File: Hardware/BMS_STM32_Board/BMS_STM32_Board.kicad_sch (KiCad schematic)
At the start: 46 parts, among them J1 Conn_01x05, J2 Conn_01x02, J3 Conn_01x04, J4 Conn_01x02, J5 Conn_01x04, Q1 Q_PMOS_GSD, U1 STM32F103C8Tx, U3 INA181, Y1 8MHz

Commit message: Hardware: footprint assignment complete
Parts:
- removed Q1: Q_PMOS_GSD, symbol Transistor_FET:Q_PMOS_GSD
- added Q1: Q_PMOS_GDS, Package_TO_SOT_SMD:TO-252-3_TabPin2, symbol Transistor_FET:Q_PMOS_GDS
- C1, C10, C11, C12, C13, C14, C15, C2, C3, C4, C6, C7, C8: footprint (none) -> Capacitor_SMD:C_0603_1608Metric
- C5: footprint (none) -> Capacitor_SMD:C_0805_2012Metric
- C9: footprint (none) -> Capacitor_THT:CP_Radial_D6.3mm_P2.50mm
- D1: footprint (none) -> Diode_SMD:D_SMA
- D2, D3, D4, D5: footprint (none) -> LED_SMD:LED_0805_2012Metric
- FB1: footprint (none) -> Inductor_SMD:L_0603_1608Metric
- J1: footprint (none) -> Connector_PinHeader_2.54mm:PinHeader_1x05_P2.54mm_Vertical
- J2, J4: footprint (none) -> TerminalBlock_Phoenix:TerminalBlock_Phoenix_MKDS-3-2-5.08_1x02_P5.08mm_Horizontal
- J3, J5: footprint (none) -> Connector:FanPinHeader_1x04_P2.54mm_Vertical
- R1, R10, R11, R12, R13, R14, R15, R2, R4, R5, R6, R7, R8, R9: footprint (none) -> Resistor_SMD:R_0603_1608Metric
- R3: footprint (none) -> Resistor_SMD:R_2512_6332Metric
- TH1: footprint (none) -> Connector_PinHeader_2.54mm:PinHeader_1x02_P2.54mm_Vertical
- Y1: footprint (none) -> Crystal:Crystal_SMD_3225-4Pin_3.2x2.5mm
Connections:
- net VIN_PROT: now also Q1.2 (D)
- net at R2.1: now also Q1.1 (G)
- net at J2.1 (Pin_1): now also Q1.3 (S)
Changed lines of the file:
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@@
 			)
 		)
-		(property "Footprint" ""
+		(property "Footprint" "Crystal:Crystal_SMD_3225-4Pin_3.2x2.5mm"
 			(at 107.95 73.66 0)
 			(hide yes)
@@
 			)
 		)
-		(property "Footprint" ""
+		(property "Footprint" "Resistor_SMD:R_0603_1608Metric"
 			(at 93.98 84.582 90)
 			(hide yes)
@@
 			)
 		)
-		(property "Footprint" ""
+		(property "Footprint" "Resistor_SMD:R_2512_6332Metric"
 			(at 58.42 103.378 90)
 			(hide yes)
@@
 			)
 		)
-		(property "Footprint" ""
+		(property "Footprint" "Resistor_SMD:R_0603_1608Metric"
 			(at 56.642 152.4 90)
 			(hide yes)
@@
 			)
 		)
-		(property "Footprint" ""
+		(property "Footprint" "Resistor_SMD:R_0603_1608Metric"
 			(at 115.062 54.61 90)
 			(hide yes)
@@
 			)
 		)
-		(property "Footprint" ""
+		(property "Footprint" "Connector:FanPinHeader_1x04_P2.54mm_Vertical"
 			(at 113.03 104.14 0)
 			(hide yes)
@@
 	)
 	(symbol
-		(lib_id "Transistor_FET:Q_PMOS_GSD")
-		(at 73.66 148.59 0)
-		(unit 1)
-		(body_style 1)
-		(exclude_from_sim no)
-		(in_bom yes)
-		(on_board yes)
-		(in_pos_files yes)
-		(dnp no)
-		(fields_autoplaced yes)
-		(property "Reference" "Q1"
-			(at 80.01 147.3199 0)
-			(show_name no)
-			(do_not_autoplace no)
-			(effects
-				(font
-					(size 1.27 1.27)
-				)
-				(justify left)
-			)
-		)
-		(property "Value" "Q_PMOS_GSD"
-			(at 80.01 149.8599 0)
-			(show_name no)
-			(do_not_autoplace no)
-			(effects
-				(font
-					(size 1.27 1.27)
-				)
-				(justify left)
-			)
-		)
-		(property "Footprint" ""
-			(at 78.74 146.05 0)
-			(hide yes)
-			(show_name no)
-			(do_not_autoplace no)
-			(effects
-				(font
-					(size 1.27 1.27)
-				)
-			)
-		)
-		(property "Datasheet" ""
-			(at 73.66 148.59 0)
-			(hide yes)
-			(show_name no)
-			(do_not_autoplace no)
-			(effects
-				(font
-					(size 1.27 1.27)
-				)
-			)
-		)
-		(property "Description" "P-MOSFET transistor, gate/source/drain"
-			(at 73.66 148.59 0)
-			(hide yes)
-			(show_name no)
-			(do_not_autoplace no)
-			(effects
-				(font
-					(size 1.27 1.27)
-				)
-			)
-		)
-		(pin "2"
-		)
-		(pin "3"
-		)
-		(pin "1"
-		)
-		(instances
-			(project "BMS_STM32_Board"
-				(path "/49c11c37-c968-4efe-b9c6-d4384c4cec3d"
-					(reference "Q1")
-					(unit 1)
-				)
-			)
-		)
-	)
-	(symbol
 		(lib_id "power:PWR_FLAG")
 		(at 266.7 158.75 0)
@@
 			)
 		)
-		(property "Footprint" ""
+		(property "Footprint" "Capacitor_SMD:C_0805_2012Metric"
 			(at 106.68 30.48 0)
 			(hide yes)
@@
 			)
 		)
-		(property "Footprint" ""
+		(property "Footprint" "Resistor_SMD:R_0603_1608Metric"
 			(at 85.852 91.44 90)
 			(hide yes)
@@
 			)
 		)
-		(property "Footprint" ""
+		(property "Footprint" "Capacitor_SMD:C_0603_1608Metric"
 			(at 116.84 30.48 0)
 			(hide yes)
@@
 			)
 		)
-		(property "Footprint" ""
+		(property "Footprint" "Capacitor_SMD:C_0603_1608Metric"
 			(at 129.54 30.48 0)
 			(hide yes)
@@
 			)
 		)
-		(property "Footprint" ""
+		(property "Footprint" "TerminalBlock_Phoenix:TerminalBlock_Phoenix_MKDS-3-2-5.08_1x02_P5.08mm_Horizontal"
 			(at 81.28 161.29 0)
 			(hide yes)
@@
 			)
 		)
-		(property "Footprint" ""
+		(property "Footprint" "Capacitor_SMD:C_0603_1608Metric"
 			(at 124.46 57.15 0)
 			(hide yes)
@@
 			)
 		)
-		(property "Footprint" ""
+		(property "Footprint" "Resistor_SMD:R_0603_1608Metric"
 			(at 152.4 81.788 90)
 			(hide yes)
@@
 			)
 		)
-		(property "Footprint" ""
+		(property "Footprint" "Resistor_SMD:R_0603_1608Metric"
 			(at 99.06 127.762 90)
 			(hide yes)
@@
 			)
 		)
-		(property "Footprint" ""
+		(property "Footprint" "Capacitor_SMD:C_0603_1608Metric"
 			(at 114.3 133.35 0)
 			(hide yes)
@@
 			)
 		)
-		(property "Footprint" ""
+		(property "Footprint" "Resistor_SMD:R_0603_1608Metric"
 			(at 211.582 53.34 90)
 			(hide yes)
@@
 			)
 		)
-		(property "Footprint" ""
+		(property "Footprint" "Capacitor_SMD:C_0603_1608Metric"
 			(at 64.77 68.58 0)
 			(hide yes)
@@
 			)
 		)
-		(property "Footprint" ""
+		(property "Footprint" "Capacitor_SMD:C_0603_1608Metric"
 			(at 92.71 67.31 0)
 			(hide yes)
@@
 			)
 		)
-		(property "Footprint" ""
+		(property "Footprint" "Resistor_SMD:R_0603_1608Metric"
 			(at 104.902 133.35 90)
 			(hide yes)
@@
 			)
 		)
-		(property "Footprint" ""
+		(property "Footprint" "Diode_SMD:D_SMA"
 			(at 85.09 135.89 0)
 			(hide yes)
@@
 			)
 		)
-		(property "Footprint" ""
+		(property "Footprint" "LED_SMD:LED_0805_2012Metric"
 			(at 142.24 80.01 0)
 			(hide yes)
@@
 			)
 		)
-		(property "Footprint" ""
+		(property "Footprint" "LED_SMD:LED_0805_2012Metric"
 			(at 182.88 152.4 0)
 			(hide yes)
@@
 			)
 		)
-		(property "Footprint" ""
+		(property "Footprint" "Resistor_SMD:R_0603_1608Metric"
 			(at 193.04 150.622 90)
 			(hide yes)
@@
 			)
 		)
-		(property "Footprint" ""
+		(property "Footprint" "Resistor_SMD:R_0603_1608Metric"
 			(at 131.318 157.48 90)
 			(hide yes)
@@
 			)
 		)
-		(property "Footprint" ""
+		(property "Footprint" "Resistor_SMD:R_0603_1608Metric"
 			(at 154.94 124.968 90)
 			(hide yes)
@@
 			)
 		)
-		(property "Footprint" ""
+		(property "Footprint" "Inductor_SMD:L_0603_1608Metric"
 			(at 179.832 45.72 90)
 			(hide yes)
@@
 			)
 		)
-		(property "Footprint" ""
+		(property "Footprint" "Resistor_SMD:R_0603_1608Metric"
 			(at 120.65 164.592 90)
 			(hide yes)
@@
 			)
 		)
-		(property "Footprint" ""
+		(property "Footprint" "Resistor_SMD:R_0603_1608Metric"
 			(at 88.9 75.692 90)
 			(hide yes)
@@
 			)
 		)
-		(property "Footprint" ""
+		(property "Footprint" "Capacitor_SMD:C_0603_1608Metric"
 			(at 142.24 30.48 0)
 			(hide yes)
@@
 			)
 		)
-		(property "Footprint" ""
+		(property "Footprint" "Resistor_SMD:R_0603_1608Metric"
 			(at 152.4 123.952 90)
 			(hide yes)
@@
 			)
 		)
-		(property "Footprint" ""
+		(property "Footprint" "Connector_PinHeader_2.54mm:PinHeader_1x05_P2.54mm_Vertical"
 			(at 209.55 97.79 0)
 			(hide yes)
@@
 			)
 		)
-		(property "Footprint" ""
+		(property "Footprint" "Capacitor_THT:CP_Radial_D6.3mm_P2.50mm"
 			(at 73.66 134.9248 0)
 			(hide yes)
@@
 			)
 		)
-		(property "Footprint" ""
+		(property "Footprint" "Capacitor_SMD:C_0603_1608Metric"
 			(at 142.24 154.94 0)
 			(hide yes)
@@
 			)
 		)
-		(property "Footprint" ""
+		(property "Footprint" "LED_SMD:LED_0805_2012Metric"
 			(at 139.7 125.73 0)
 			(hide yes)
@@
 			)
 		)
-		(property "Footprint" ""
+		(property "Footprint" "Capacitor_SMD:C_0603_1608Metric"
 			(at 111.76 64.77 0)
 			(hide yes)
@@
 			)
 		)
-		(property "Footprint" ""
+		(property "Footprint" "LED_SMD:LED_0805_2012Metric"
 			(at 147.32 123.19 0)
 			(hide yes)
@@
 			)
 		)
-		(property "Footprint" ""
+		(property "Footprint" "Connector:FanPinHeader_1x04_P2.54mm_Vertical"
 			(at 142.24 161.29 0)
 			(hide yes)
@@
 			)
 		)
-		(property "Footprint" ""
+		(property "Footprint" "Capacitor_SMD:C_0603_1608Metric"
 			(at 233.68 64.77 0)
 			(hide yes)
@@
 			)
 		)
-		(property "Footprint" ""
+		(property "Footprint" "Capacitor_SMD:C_0603_1608Metric"
 			(at 82.55 91.44 0)
 			(hide yes)
@@
 			)
 		)
-		(property "Footprint" ""
+		(property "Footprint" "Connector_PinHeader_2.54mm:PinHeader_1x02_P2.54mm_Vertical"
 			(at 213.36 67.31 0)
 			(hide yes)
@@
 			)
 		)
-		(property "Footprint" ""
+		(property "Footprint" "Capacitor_SMD:C_0603_1608Metric"
 			(at 154.94 30.48 0)
 			(hide yes)
@@
 	)
 	(symbol
+		(lib_id "Transistor_FET:Q_PMOS_GDS")
+		(at 73.66 148.59 0)
+		(unit 1)
+		(body_style 1)
+		(exclude_from_sim no)
+		(in_bom yes)
+		(on_board yes)
+		(in_pos_files yes)
+		(dnp no)
+		(fields_autoplaced yes)
+		(property "Reference" "Q1"
+			(at 80.01 147.3199 0)
+			(show_name no)
+			(do_not_autoplace no)
+			(effects
+				(font
+					(size 1.27 1.27)
+				)
+				(justify left)
+			)
+		)
+		(property "Value" "Q_PMOS_GDS"
+			(at 80.01 149.8599 0)
+			(show_name no)
+			(do_not_autoplace no)
+			(effects
+				(font
+					(size 1.27 1.27)
+				)
+				(justify left)
+			)
+		)
+		(property "Footprint" "Package_TO_SOT_SMD:TO-252-3_TabPin2"
+			(at 78.74 146.05 0)
+			(hide yes)
+			(show_name no)
+			(do_not_autoplace no)
+			(effects
+				(font
+					(size 1.27 1.27)
+				)
+			)
+		)
+		(property "Datasheet" ""
+			(at 73.66 148.59 0)
+			(hide yes)
+			(show_name no)
+			(do_not_autoplace no)
+			(effects
+				(font
+					(size 1.27 1.27)
+				)
+			)
+		)
+		(property "Description" "P-MOSFET transistor, gate/drain/source"
+			(at 73.66 148.59 0)
+			(hide yes)
+			(show_name no)
+			(do_not_autoplace no)
+			(effects
+				(font
+					(size 1.27 1.27)
+				)
+			)
+		)
+		(pin "1"
+		)
+		(pin "2"
+		)
+		(pin "3"
+		)
+		(instances
+			(project "BMS_STM32_Board"
+				(path "/49c11c37-c968-4efe-b9c6-d4384c4cec3d"
+					(reference "Q1")
+					(unit 1)
+				)
+			)
+		)
+	)
+	(symbol
 		(lib_id "Connector_Generic:Conn_01x02")
 		(at 38.1 101.6 0)
@@
 			)
 		)
-		(property "Footprint" ""
+		(property "Footprint" "TerminalBlock_Phoenix:TerminalBlock_Phoenix_MKDS-3-2-5.08_1x02_P5.08mm_Horizontal"
 			(at 38.1 101.6 0)
 			(hide yes)
@@
 			)
 		)
-		(property "Footprint" ""
+		(property "Footprint" "Capacitor_SMD:C_0603_1608Metric"
 			(at 111.76 82.55 0)
 			(hide yes)

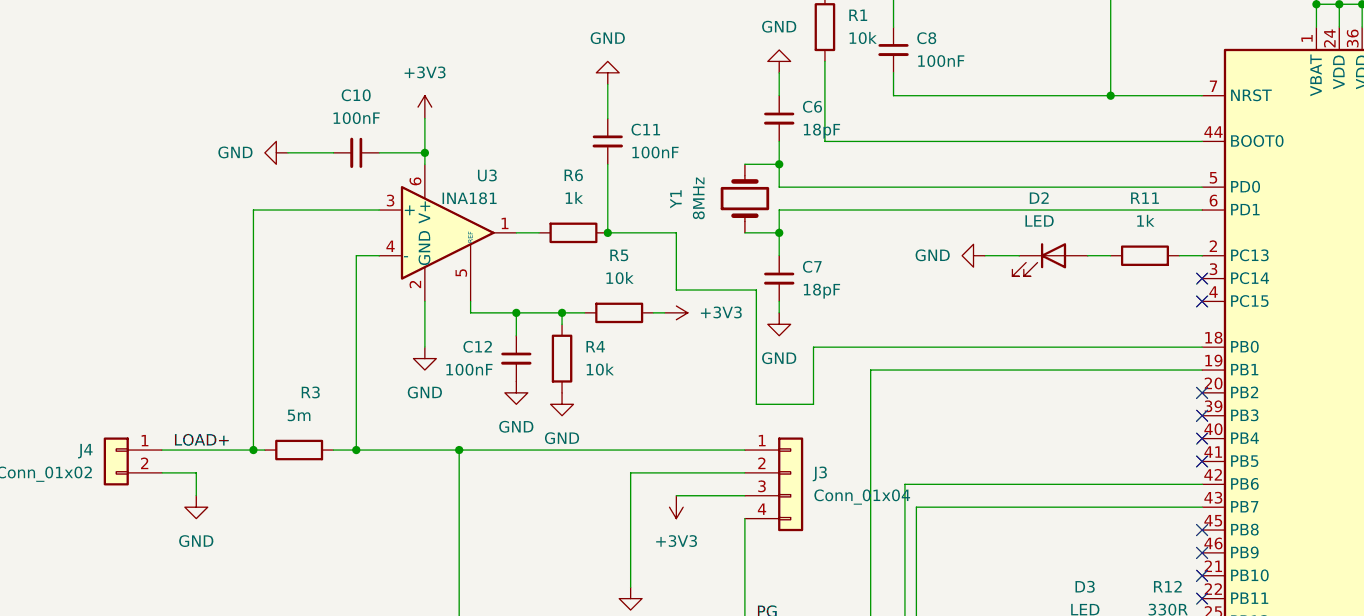
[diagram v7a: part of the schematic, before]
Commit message: Hardware: footprint fixes (crystal GND24, pin headers), PCB import clean
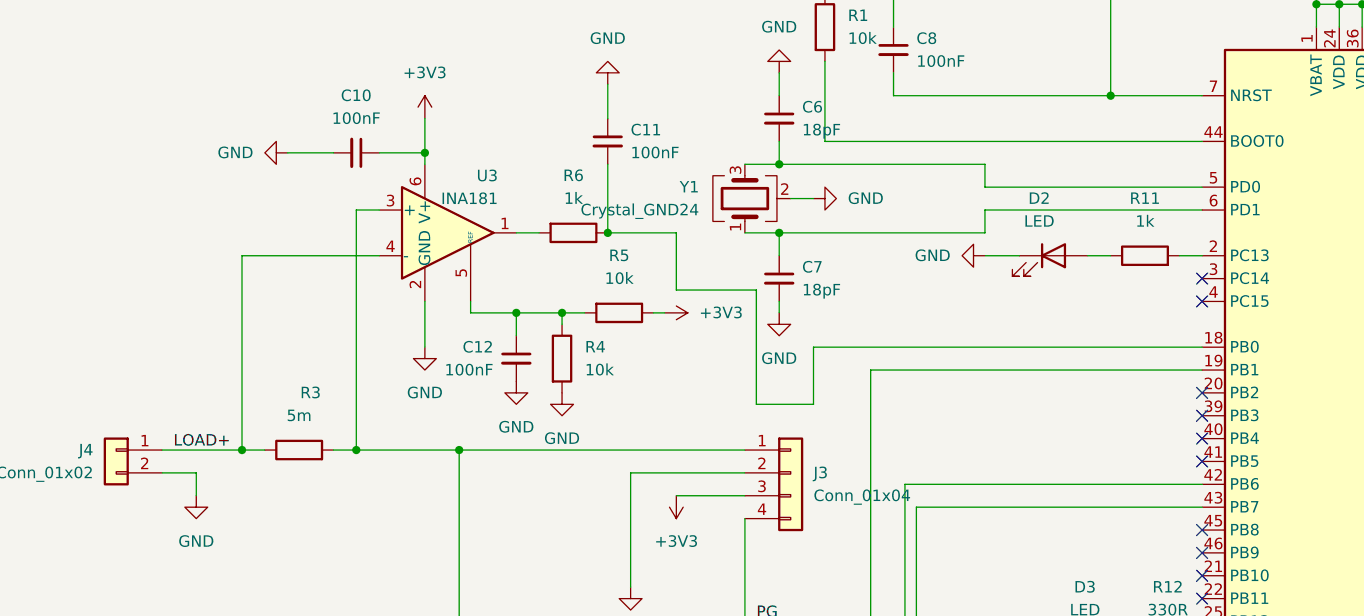
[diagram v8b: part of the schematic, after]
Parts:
- removed Y1: 8MHz, Crystal:Crystal_SMD_3225-4Pin_3.2x2.5mm, symbol Device:Crystal
- added Y1: Crystal_GND24, Crystal:Crystal_SMD_3225-4Pin_3.2x2.5mm, symbol Device:Crystal_GND24
- J3, J5: footprint Connector:FanPinHeader_1x04_P2.54mm_Vertical -> Connector_PinHeader_2.54mm:PinHeader_1x04_P2.54mm_Vertical
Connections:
- net GND: now also Y1.2 (G), Y1.4 (G)
- net LOAD+: now also U3.4 (-); no longer U3.3 (+)
- net VIN_PROT: now also U3.3 (+); no longer U3.4 (-)
- net at C7.1, U1.6 (PD1): now also Y1.1
- net at C6.2, U1.5 (PD0): now also Y1.3
